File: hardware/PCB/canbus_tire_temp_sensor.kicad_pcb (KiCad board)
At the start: 2 copper layers, 40 x 20 mm, 40 parts, among them J1 TC2030, J2 0430450423, U1 TLE42744DV33ATMA1, U2 STM32F042K6Ux, U3 MLX90641ESF-BCA-000-SP, U4 TCAN3403DRQ1, Y1 ECS-160-10-36Q-AES-TR

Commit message: Initial board layout
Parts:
- added C10: 10nF, Capacitor_SMD:C_0603_1608Metric, F.Cu at (156.2, 97.0)
- added C12: 1uF, Capacitor_SMD:C_0603_1608Metric, F.Cu at (159.2, 97.0)
- C14: renamed from C12; moved to B.Cu
- D1: value SMBJ36CA-13-F -> SMBJ36CA-13-F
- moved TP4 8.87 mm to (162.2, 91.2)
- moved TP1 7.95 mm to (132.2, 92.2)
- moved TP3 3.26 mm to (162.2, 95.2)
- moved C14 2.30 mm to (151.8, 95.5), turned to -90 degrees
- moved C2 1.77 mm to (164.2, 96.2)
- moved C7 1.77 mm to (165.8, 96.2)
- moved R4 1.50 mm to (143.0, 108.5)
- moved R5 1.50 mm to (143.0, 107.0)
- moved TP5 1.21 mm to (151.4, 105.5)
- moved TP6 1.21 mm to (148.6, 105.5)
- moved D2 1.00 mm to (134.5, 108.0)
- moved JP1 0.90 mm to (166.2, 108.5)
- moved TP2 0.25 mm to (139.8, 104.5)
- moved C1 0.20 mm to (162.8, 106.0)
- moved C3 0.20 mm to (160.8, 108.5)
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- renumbered C10 to C11, C11 to C13, C13 to C15, C14 to C16
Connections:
- net /CANH renamed /CAN_P
- net /CANL renamed /CAN_N
- R4 pad 1: /S1 -> /LED_STATUS_1
- R5 pad 1: /S2 -> /LED_STATUS_2
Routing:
- net +3V3: track 0.00 -> 118.3 mm, vias 0 -> 4
- net GND: track 0.00 -> 25.0 mm, vias 0 -> 49
- net /CAN_P: track 0.00 -> 24.9 mm
- net /CAN_N: track 0.00 -> 24.9 mm
- net /NRST: track 0.00 -> 18.2 mm, vias 0 -> 2
- net /LED_STATUS_1: track 0.00 -> 17.7 mm
- net /LED_STATUS_2: track 0.00 -> 17.0 mm
- net /CAN_RX: track 0.00 -> 16.8 mm, vias 0 -> 2
- net /SCL: track 0.00 -> 16.1 mm
- net VCC: track 0.00 -> 15.3 mm
- net /BOOT0: track 0.00 -> 14.8 mm
- net /CAN_TX: track 0.00 -> 13.2 mm, vias 0 -> 2
- net /SDA: track 0.00 -> 12.4 mm
- net /CAN_STANDBY: track 0.00 -> 9.14 mm, vias 0 -> 2
- net Net-(D2-A): track 0.00 -> 8.38 mm
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- added copper zone on B.Cu, net GND
- added copper zone on F.Cu, net GND
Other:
- board text added: "3.3V"
- board text added: "BOOT"
- board text added: "Brian Glen 2025"
- board text added: "CAN H"
- board text added: "CAN L"
- board text added: "Config Message: 0x710"
- board text added: "Data Message: 0x700 + 1, 2, 3"
- board text added: "Default CAN ID:"
- board text added: "G"
- board text added: "GND"
- board text added: "Input: 4.5 - 40 VDC"
- board text added: "RX"
- board text added: "SCL"
- board text added: "SDA"
- board text added: "TX"
- board text added: "Tire Thermal Camera"
- board text added: "V"
- board text added: "VCC"

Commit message: gerbers version 1.0
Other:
- board text added: "Version 1.0"
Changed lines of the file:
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@@
+		)
+	)
+	(gr_text "Version 1.0"
+		(at 169 95.25 0)
+		(layer "B.SilkS")
+		(effects
+			(font
+				(size 1 1)
+				(thickness 0.15)
+			)
+			(justify left mirror)
 		)
 	)

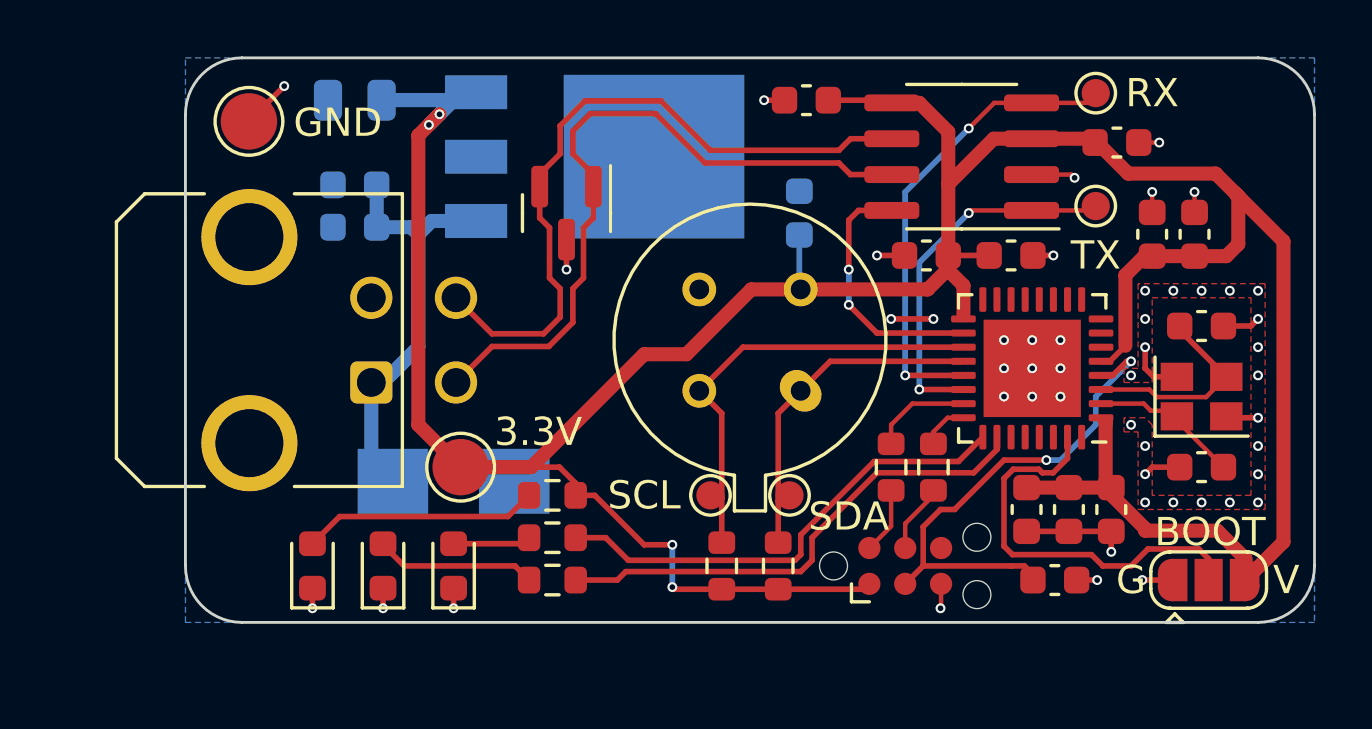
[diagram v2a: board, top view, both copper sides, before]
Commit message: Updated connector, fixed MLX footprint
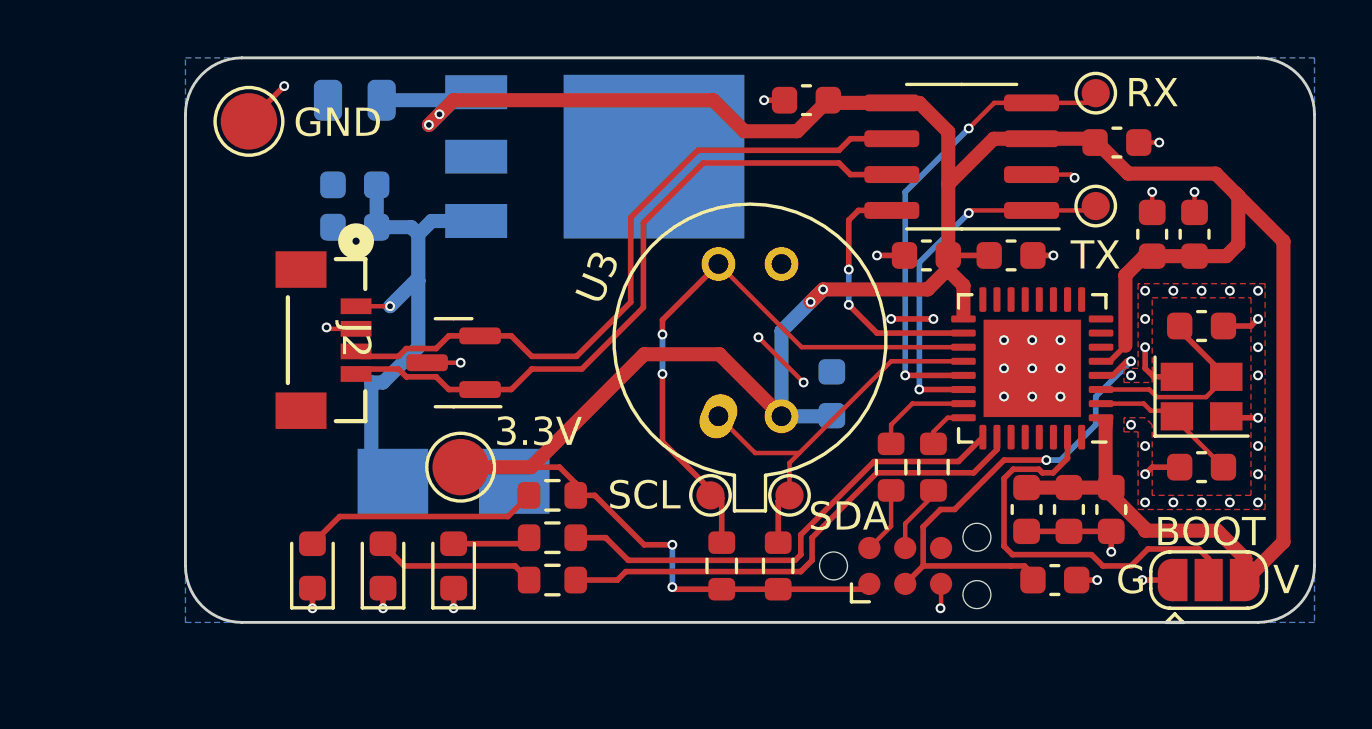
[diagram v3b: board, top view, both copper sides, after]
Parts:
- J2: value 0430450423 -> 2147210040; footprint Connector_Molex:Molex_Micro-Fit_3.0_43045-0421_2x02-1MP_P3.00mm_Horizontal -> canbus_tire_temp_sensor:Molex_Zero_Hatchi_2147210040
- U3: footprint Package_TO_SOT_THT:TO-39-4_Window -> canbus_tire_temp_sensor:MLX90641
- moved D5 6.64 mm to (139.5, 100.8), turned to 180 degrees
- moved C14 6.50 mm to (152.9, 101.9)
- moved U3 2.54 mm to (150.0, 100.0), turned to 67.5 degrees
- moved J2 2.18 mm to (135.0, 100.0), turned to -90 degrees
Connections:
- J2 pad 3: /CAN_P -> /CAN_N
- J2 pad 4: /CAN_N -> /CAN_P
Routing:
- net +3V3: track 118.3 -> 124.4 mm, vias 4 -> 6
- net /SCL: track 16.1 -> 21.6 mm, vias 0 -> 2
- net GND: track 25.0 -> 28.4 mm, vias 49 -> 52
- net VCC: track 15.3 -> 17.9 mm, vias 0 -> 1
- net /SDA: track 12.4 -> 14.2 mm
